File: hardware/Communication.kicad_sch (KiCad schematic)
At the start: 28 parts, among them J1 Conn_01x04_Pin, J2 Conn_01x03_Male, J3 USB_C_Receptacle_USB2.0, U21 TXB0102DCT, U22 ADUM4160

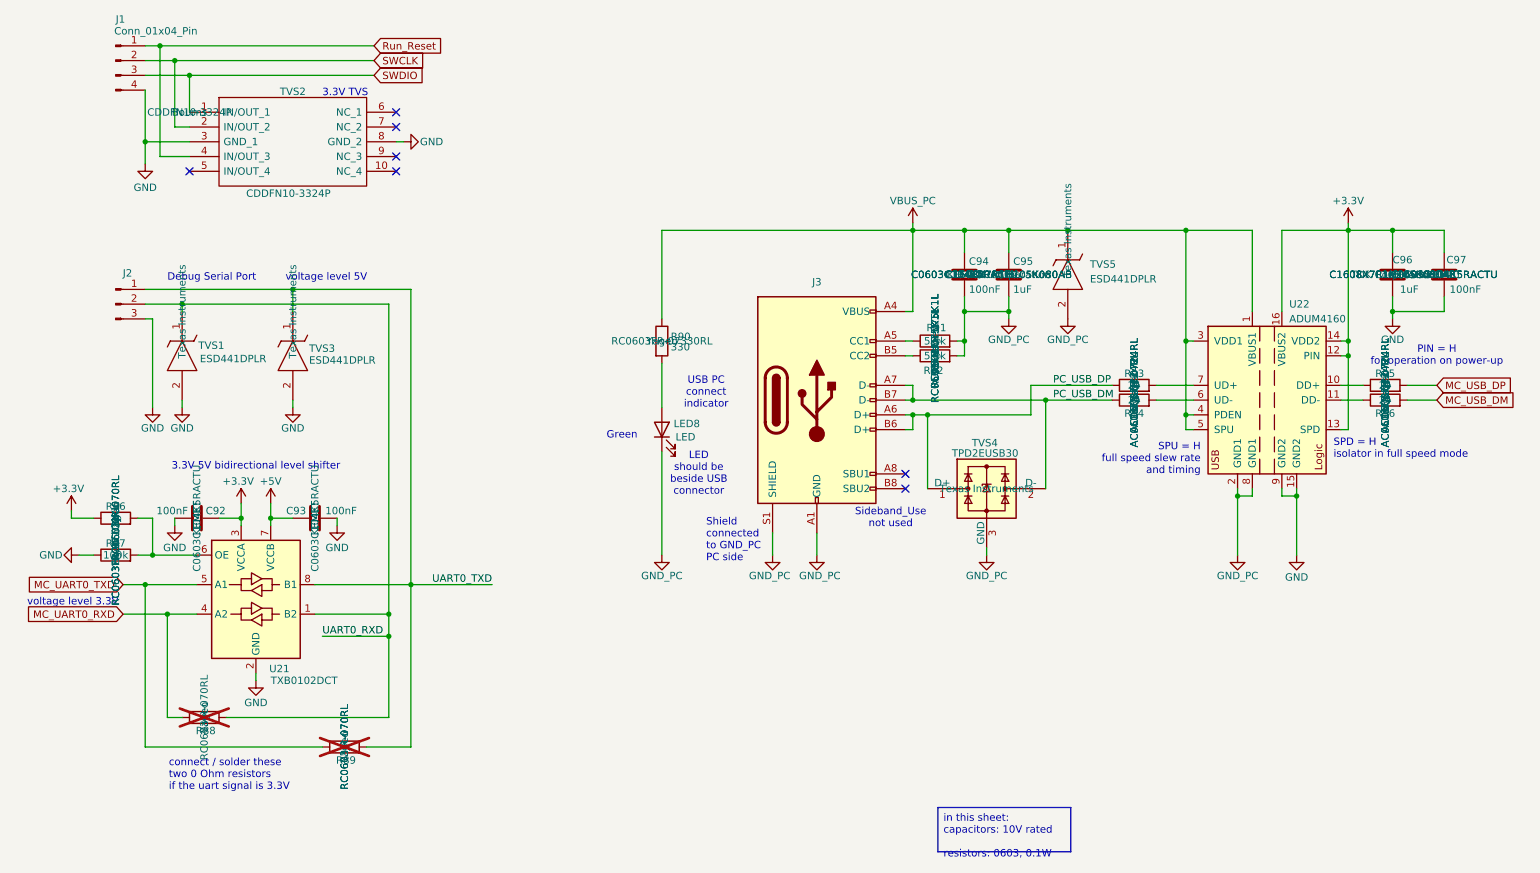
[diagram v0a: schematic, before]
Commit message: Not necessary text is hidden + BOM on schematic
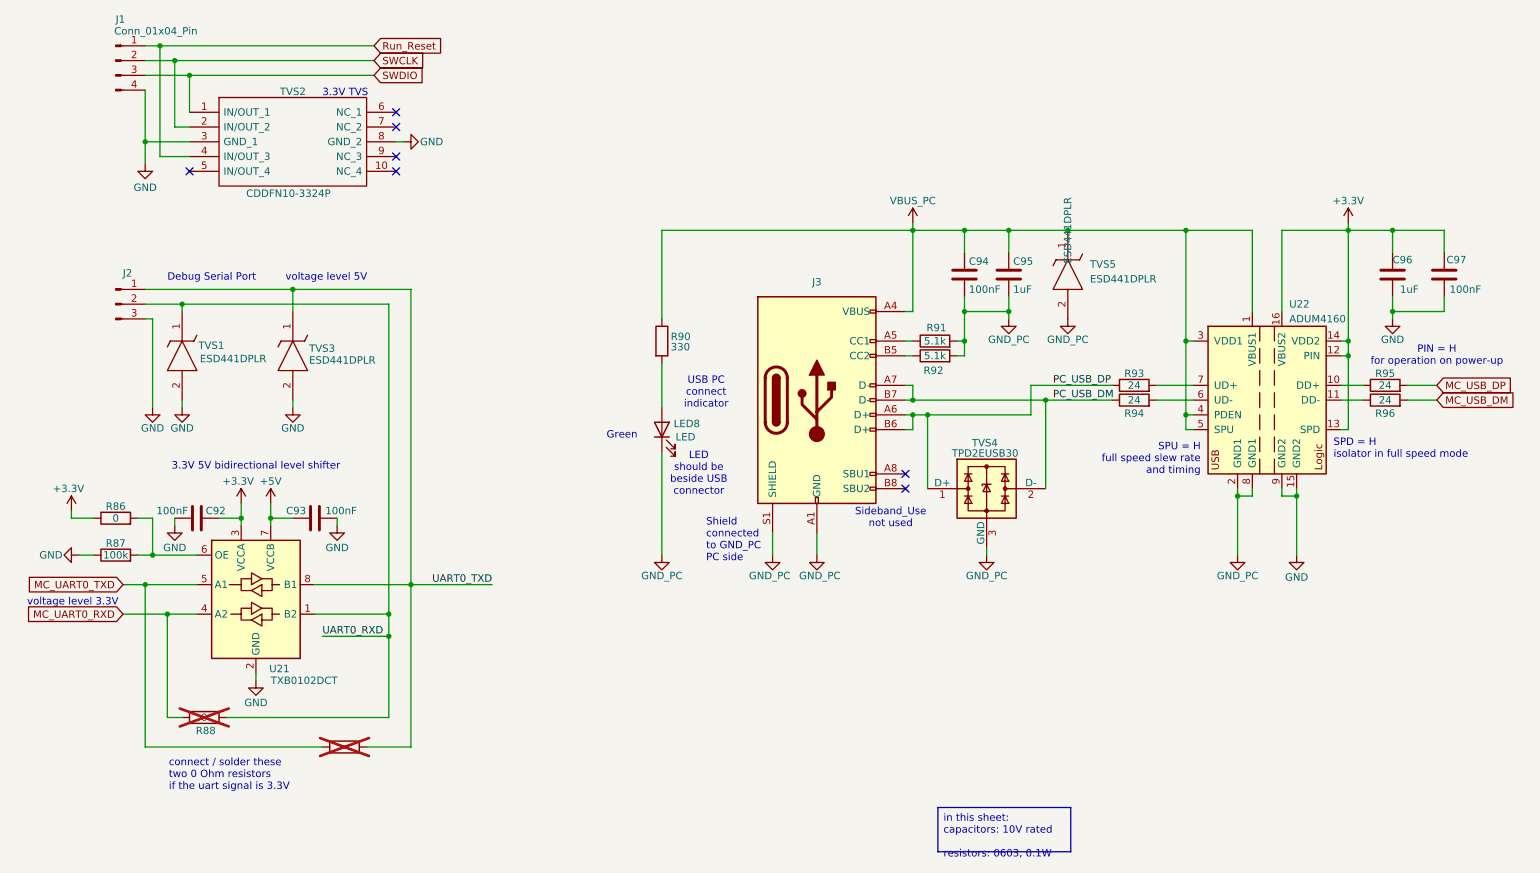
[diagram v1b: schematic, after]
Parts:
- C92, C93, C94, C97: Temperature Coefficient X7R -> (none)
- C95, C96: Temperature Coefficient X5R -> (none)
- LED8: Manufacturer_Part_Number (none) -> XZCDGK53W-1VF
- TVS1, TVS3, TVS5: MPN (none) -> ESD441DPLR
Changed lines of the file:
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@@
 					(size 1.27 1.27)
 				)
+				(hide yes)
 			)
 		)
@@
 					(size 1.27 1.27)
 				)
+				(hide yes)
 			)
 		)
@@
 					(size 1.27 1.27)
 				)
+				(hide yes)
 			)
 		)
@@
 					(size 1.27 1.27)
 				)
+				(hide yes)
 			)
 		)
@@
 					(size 1.27 1.27)
 				)
+				(hide yes)
 			)
 		)
@@
 					(size 1.27 1.27)
 				)
+				(hide yes)
 			)
 		)
@@
 					(size 1.27 1.27)
 				)
+				(hide yes)
+			)
+		)
+		(property "MPN" "ESD441DPLR"
+			(at 46.99 72.39 0)
+			(effects
+				(font
+					(size 1.27 1.27)
+				)
+				(hide yes)
 			)
 		)
@@
 					(size 1.27 1.27)
 				)
+				(hide yes)
+			)
+		)
+		(property "MPN" "ESD441DPLR"
+			(at 66.04 72.39 0)
+			(effects
+				(font
+					(size 1.27 1.27)
+				)
+				(hide yes)
 			)
 		)
@@
 					(size 1.27 1.27)
 				)
+				(hide yes)
 			)
 		)
@@
 					(size 1.27 1.27)
 				)
+				(hide yes)
 			)
 		)
@@
 					(size 1.27 1.27)
 				)
+				(hide yes)
 			)
 		)
@@
 			)
 		)
-		(property "Temperature Coefficient" "X7R"
+		(property "Temperature Coefficient" ""
 			(at 49.53 107.95 0)
 			(effects
@@
 					(size 1.27 1.27)
 				)
+				(hide yes)
 			)
 		)
@@
 					(size 1.27 1.27)
 				)
+				(hide yes)
 			)
 		)
@@
 					(size 1.27 1.27)
 				)
+				(hide yes)
 			)
 		)
@@
 					(size 1.27 1.27)
 				)
+				(hide yes)
+			)
+		)
+		(property "MPN" "ESD441DPLR"
+			(at 199.39 58.42 0)
+			(effects
+				(font
+					(size 1.27 1.27)
+				)
 			)
 		)
@@
 					(size 1.27 1.27)
 				)
+				(hide yes)
 			)
 		)
@@
 					(size 1.27 1.27)
 				)
+				(hide yes)
 			)
 		)
@@
 					(size 1.27 1.27)
 				)
+				(hide yes)
 			)
 		)
@@
 					(size 1.27 1.27)
 				)
+				(hide yes)
 			)
 		)
@@
 					(size 1.27 1.27)
 				)
+				(hide yes)
 			)
 		)
@@
 					(size 1.27 1.27)
 				)
+				(hide yes)
 			)
 		)
@@
 					(size 1.27 1.27)
 				)
+				(hide yes)
 			)
 		)
@@
 					(size 1.27 1.27)
 				)
+				(hide yes)
 			)
 		)
@@
 					(size 1.27 1.27)
 				)
+				(hide yes)
 			)
 		)
@@
 					(size 1.27 1.27)
 				)
+				(hide yes)
 			)
 		)
@@
 					(size 1.27 1.27)
 				)
+				(hide yes)
 			)
 		)
@@
 					(size 1.27 1.27)
 				)
+				(hide yes)
 			)
 		)
@@
 					(size 1.27 1.27)
 				)
+				(hide yes)
 			)
 		)
@@
 					(size 1.27 1.27)
 				)
+				(hide yes)
 			)
 		)
@@
 			)
 		)
-		(property "Temperature Coefficient" "X7R"
+		(property "Temperature Coefficient" ""
 			(at 264.16 66.04 0)
 			(effects
@@
 					(size 1.27 1.27)
 				)
+				(hide yes)
 			)
 		)
@@
 					(size 1.27 1.27)
 				)
+				(hide yes)
 			)
 		)
@@
 					(size 1.27 1.27)
 				)
+				(hide yes)
 			)
 		)
@@
 					(size 1.27 1.27)
 				)
+				(hide yes)
 			)
 		)
@@
 					(size 1.27 1.27)
 				)
+				(hide yes)
 			)
 		)
@@
 					(size 1.27 1.27)
 				)
+				(hide yes)
 			)
 		)
@@
 					(size 1.27 1.27)
 				)
+				(hide yes)
 			)
 		)
@@
 					(size 1.27 1.27)
 				)
+				(hide yes)
 			)
 		)
@@
 					(size 1.27 1.27)
 				)
+				(hide yes)
 			)
 		)
@@
 					(size 1.27 1.27)
 				)
+				(hide yes)
 			)
 		)
@@
 			)
 		)
-		(property "Temperature Coefficient" "X5R"
+		(property "Temperature Coefficient" ""
 			(at 255.27 66.04 0)
 			(effects
@@
 					(size 1.27 1.27)
 				)
+				(hide yes)
 			)
 		)
@@
 					(size 1.27 1.27)
 				)
+				(hide yes)
 			)
 		)
@@
 					(size 1.27 1.27)
 				)
+				(hide yes)
 			)
 		)
@@
 					(size 1.27 1.27)
 				)
+				(hide yes)
 			)
 		)
@@
 					(size 1.27 1.27)
 				)
+				(hide yes)
 			)
 		)
@@
 					(size 1.27 1.27)
 				)
+				(hide yes)
 			)
 		)
@@
 					(size 1.27 1.27)
 				)
+				(hide yes)
 			)
 		)
@@
 			)
 		)
-		(property "Temperature Coefficient" "X7R"
+		(property "Temperature Coefficient" ""
 			(at 181.61 66.04 0)
 			(effects
@@
 					(size 1.27 1.27)
 				)
+				(hide yes)
 			)
 		)
@@
 					(size 1.27 1.27)
 				)
+				(hide yes)
 			)
 		)
@@
 					(size 1.27 1.27)
 				)
+				(hide yes)
 			)
 		)
@@
 			)
 		)
+		(property "Manufacturer_Part_Number" "XZCDGK53W-1VF"
+			(at 126.746 92.456 0)
+			(effects
+				(font
+					(size 1.27 1.27)
+				)
+				(hide yes)
+			)
+		)
 		(pin "1"
 		)
@@
 			)
 		)
-		(property "Temperature Coefficient" "X5R"
+		(property "Temperature Coefficient" ""
 			(at 189.23 66.04 0)
 			(effects
@@
 					(size 1.27 1.27)
 				)
+				(hide yes)
 			)
 		)
@@
 					(size 1.27 1.27)
 				)
+				(hide yes)
 			)
 		)
@@
 					(size 1.27 1.27)
 				)
+				(hide yes)
 			)
 		)
@@
 					(size 1.27 1.27)
 				)
+				(hide yes)
 			)
 		)
@@
 			)
 		)
-		(property "Temperature Coefficient" "X7R"
+		(property "Temperature Coefficient" ""
 			(at 69.85 107.95 0)
 			(effects
@@
 					(size 1.27 1.27)
 				)
+				(hide yes)
 			)
 		)
@@
 					(size 1.27 1.27)
 				)
+				(hide yes)
 			)
 		)
@@
 					(size 1.27 1.27)
 				)
+				(hide yes)
 			)
 		)
@@
 					(size 1.27 1.27)
 				)
+				(hide yes)
 			)
 		)

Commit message: BOM cont.
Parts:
- J1: Link (none) -> n/a; MPN (none) -> n/a; Manufacturer (none) -> n/a; Manufacturer_Name (none) -> n/a; Manufacturer_Part_Number (none) -> n/a
- J2: MPN (none) -> n/a; Manufacturer_Name (none) -> n/a; Manufacturer_Part_Number (none) -> n/a
- J3: MPN (none) -> DX07S016JA1R1500; Manufacturer_Name (none) -> JAE Electronics; Manufacturer_Part_Number (none) -> DX07S016JA1R1500
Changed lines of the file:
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@@
 	(text "voltage level 5V"
 		(exclude_from_sim no)
-		(at 64.77 67.31 0)
+		(at 70.358 68.072 0)
 		(effects
 			(font
@@
 	(text "Debug Serial Port"
 		(exclude_from_sim no)
-		(at 44.45 67.31 0)
+		(at 48.26 68.072 0)
 		(effects
 			(font
@@
 			)
 		)
+		(property "Link" "n/a"
+			(at 35.56 29.21 0)
+			(effects
+				(font
+					(size 1.27 1.27)
+				)
+				(hide yes)
+			)
+		)
+		(property "Manufacturer" "n/a"
+			(at 35.56 29.21 0)
+			(effects
+				(font
+					(size 1.27 1.27)
+				)
+				(hide yes)
+			)
+		)
+		(property "Manufacturer_Part_Number" "n/a"
+			(at 35.56 29.21 0)
+			(effects
+				(font
+					(size 1.27 1.27)
+				)
+				(hide yes)
+			)
+		)
+		(property "MPN" "n/a"
+			(at 35.56 29.21 0)
+			(effects
+				(font
+					(size 1.27 1.27)
+				)
+				(hide yes)
+			)
+		)
+		(property "Manufacturer_Name" "n/a"
+			(at 35.56 29.21 0)
+			(effects
+				(font
+					(size 1.27 1.27)
+				)
+				(hide yes)
+			)
+		)
 		(pin "2"
 		)
@@
 		(dnp no)
 		(property "Reference" "J2"
-			(at 37.592 65.786 0)
+			(at 37.084 62.484 0)
 			(effects
 				(font
@@
 		)
 		(property "Value" "Conn_01x03_Male"
-			(at 36.195 66.04 0)
+			(at 35.56 65.024 0)
 			(effects
 				(font
 					(size 1.27 1.27)
 				)
-				(hide yes)
+				(justify left)
 			)
 		)
@@
 			)
 		)
+		(property "Manufacturer_Part_Number" "n/a"
+			(at 35.56 71.12 0)
+			(effects
+				(font
+					(size 1.27 1.27)
+				)
+				(hide yes)
+			)
+		)
+		(property "MPN" "n/a"
+			(at 35.56 71.12 0)
+			(effects
+				(font
+					(size 1.27 1.27)
+				)
+				(hide yes)
+			)
+		)
+		(property "Manufacturer_Name" "n/a"
+			(at 35.56 71.12 0)
+			(effects
+				(font
+					(size 1.27 1.27)
+				)
+				(hide yes)
+			)
+		)
 		(pin "1"
 		)
@@
 		(on_board yes)
 		(dnp no)
-		(fields_autoplaced yes)
 		(property "Reference" "J3"
 			(at 156.21 67.31 0)
@@
 		)
 		(property "Value" "USB_C_Receptacle_USB2.0"
-			(at 156.21 67.31 0)
+			(at 155.956 68.834 0)
 			(effects
 				(font
 					(size 1.27 1.27)
 				)
-				(hide yes)
 			)
 		)
@@
 			(at 156.21 87.63 0)
 			(effects
+				(font
+					(size 1.27 1.27)
+				)
+				(hide yes)
+			)
+		)
+		(property "Manufacturer_Part_Number" "DX07S016JA1R1500"
+			(at 156.21 87.63 0)
+			(effects
+				(font
+					(size 1.27 1.27)
+				)
+				(hide yes)
+			)
+		)
+		(property "MPN" "DX07S016JA1R1500"
+			(at 156.21 87.63 0)
+			(effects
+				(font
+					(size 1.27 1.27)
+				)
+				(hide yes)
+			)
+		)
+		(property "Manufacturer_Name" "JAE Electronics"
+			(at 156.21 87.63 0)
+			(effects

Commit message: TVS16,TVS17,TVS18,TVS19 parts have been changed from ESDSB12VLB-TP to PESD12VL1BSLAZ
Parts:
- TVS2: footprint CDDFN103324P -> harp.device.quad.dac.kicad:CDDFN103324P
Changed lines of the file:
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@@
 			)
 		)
-		(property "Footprint" "CDDFN103324P"
+		(property "Footprint" "harp.device.quad.dac.kicad:CDDFN103324P"
 			(at 80.01 35.56 0)
 			(effects

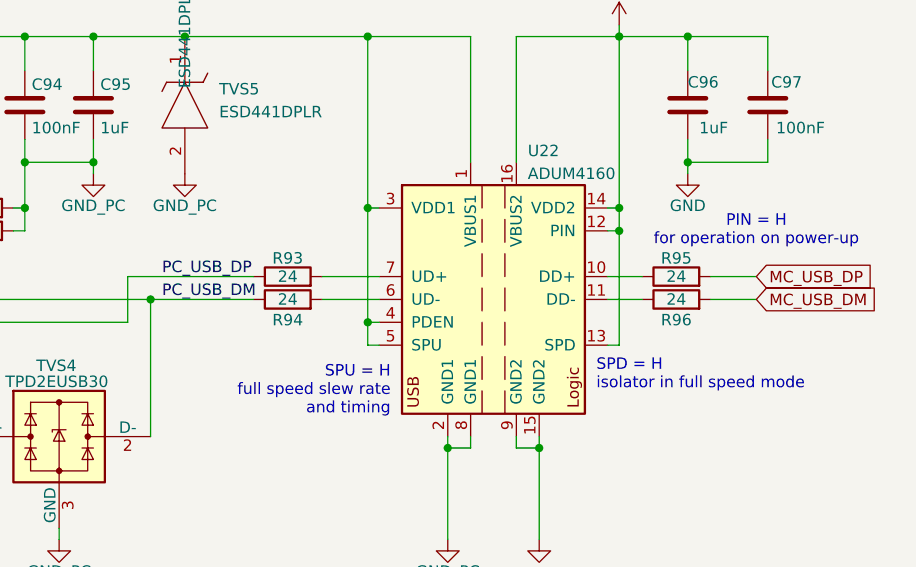
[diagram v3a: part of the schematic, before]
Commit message: Rename Some nets
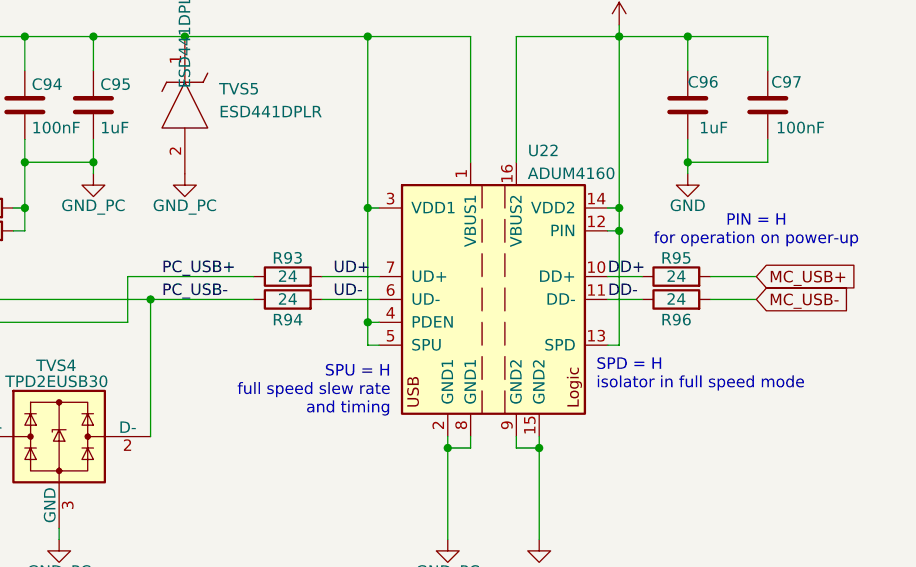
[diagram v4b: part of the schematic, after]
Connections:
- net DD-: now reaches R96.1, U22.11 (DD-)
- net UD-: now reaches R94.2, U22.6 (UD-)
- net DD+: now reaches R95.1, U22.10 (DD+)
- net UD+: now reaches R93.2, U22.7 (UD+)
- net MC_USB_DM renamed MC_USB-
- net MC_USB_DP renamed MC_USB+
- net PC_USB_DM renamed PC_USB-
- net PC_USB_DP renamed PC_USB+
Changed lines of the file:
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@@
+		)
+	)
+	(label "DD-"
+		(at 246.4062 87.63 0)
+		(effects
+			(font
+				(size 1.27 1.27)
+			)
+			(justify left bottom)
+		)
+	)
+	(label "DD+"
+		(at 246.38 85.09 0)
+		(effects
+			(font
+				(size 1.27 1.27)
+			)
+			(justify left bottom)
 		)
 	)
@@
 		)
 	)
-	(label "PC_USB_DM"
+	(label "UD+"
+		(at 215.9 85.09 0)
+		(effects
+			(font
+				(size 1.27 1.27)
+			)
+			(justify left bottom)
+		)
+	)
+	(label "PC_USB-"
 		(at 196.85 87.63 0)
 		(effects
@@
 		)
 	)
-	(label "PC_USB_DP"
+	(label "PC_USB+"
 		(at 196.85 85.09 0)
+		(effects
+			(font
+				(size 1.27 1.27)
+			)
+			(justify left bottom)
+		)
+	)
+	(label "UD-"
+		(at 215.9 87.63 0)
 		(effects
 			(font
@@
 		)
 	)
-	(global_label "MC_USB_DM"
+	(global_label "MC_USB-"
 		(shape input)
 		(at 262.89 87.63 0)
@@
 		)
 		(property "Intersheetrefs" "${INTERSHEET_REFS}"
-			(at 277.0632 87.63 0)
+			(at 274.9466 87.63 0)
 			(effects
 				(font
@@
 		)
 	)
-	(global_label "MC_USB_DP"
+	(global_label "MC_USB+"
 		(shape input)
 		(at 262.89 85.09 0)
@@
 		)
 		(property "Intersheetrefs" "${INTERSHEET_REFS}"
-			(at 276.8818 85.09 0)
+			(at 274.9466 85.09 0)
 			(effects
 				(font

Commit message: The layout is complete, and the design is currently in the review stage.
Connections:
- net SWCLK: now also J1.3 (Pin_3), TVS2.1 (IN/OUT_1); no longer J1.2 (Pin_2), TVS2.2 (IN/OUT_2)
- net SWDIO: now also J1.2 (Pin_2), TVS2.2 (IN/OUT_2); no longer J1.3 (Pin_3), TVS2.1 (IN/OUT_1)

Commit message: Continue BOM + enhance BOM + enhance schematic
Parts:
- C95, C96: Manufacturer TDK Corporation -> TDK; Manufacturer_Name TDK Corporation -> TDK
- LED8: Manufacturer_Name (none) -> SunLED
- TVS1, TVS3, TVS5: Link (none) -> https://www.digikey.com/en/products/detail/texas-instrument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
- TVS2: Link (none) -> https://www.digikey.com/en/products/detail/bourns-inc/CDDFN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
- TVS4: MPN (none) -> TPD2EUSB30DRTR; Manufacturer_Part_Number (none) -> TPD2EUSB30DRTR
- U21: value TXB0102DCT -> TXB0102DCUT; Link (none) -> https://www.digikey.com/en/products/detail/texas-instrument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; MPN (none) -> TXB0102DCUT; Manufacturer (none) -> Texas Instruments; Manufacturer_Name (none) -> Texas Instruments; Manufacturer_Part_Number (none) -> TXB0102DCUT
- U22: MPN (none) -> ADUM4160BRWZ-RL; Manufacturer Analog Devices Inc. -> Analog Devices; Manufacturer_Name (none) -> Analog Devices; Manufacturer_Part_Number (none) -> ADUM4160BRWZ-RL
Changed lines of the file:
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@@
 			)
 		)
+		(property "Link" "https://www.digikey.com/en/products/detail/texas-instruments/ESD441DPLR/21298753"
+			(at 46.99 72.39 0)
+			(effects
+				(font
+					(size 1.27 1.27)
+				)
+				(hide yes)
+			)
+		)
 		(pin "2"
 		)
@@
 			)
 		)
+		(property "Link" "https://www.digikey.com/en/products/detail/texas-instruments/ESD441DPLR/21298753"
+			(at 66.04 72.39 0)
+			(effects
+				(font
+					(size 1.27 1.27)
+				)
+				(hide yes)
+			)
+		)
 		(pin "2"
 		)
@@
 			)
 		)
+		(property "MPN" "TPD2EUSB30DRTR"
+			(at 185.42 102.87 0)
+			(effects
+				(font
+					(size 1.27 1.27)
+				)
+				(hide yes)
+			)
+		)
+		(property "Manufacturer_Part_Number" "TPD2EUSB30DRTR"
+			(at 185.42 102.87 0)
+			(effects
+				(font
+					(size 1.27 1.27)
+				)
+				(hide yes)
+			)
+		)
 		(pin "1"
 		)
@@
 					(size 1.27 1.27)
 				)
+				(hide yes)
+			)
+		)
+		(property "Link" "https://www.digikey.com/en/products/detail/texas-instruments/ESD441DPLR/21298753"
+			(at 199.39 58.42 0)
+			(effects
+				(font
+					(size 1.27 1.27)
+				)
+				(hide yes)
 			)
 		)
@@
 			)
 		)
-		(property "Value" "TXB0102DCT"
+		(property "Value" "TXB0102DCUT"
 			(at 62.23 135.89 0)
 			(effects
@@
 			)
 		)
+		(property "Link" "https://www.digikey.com/en/products/detail/texas-instruments/TXB0102DCUT/1910149"
+			(at 59.69 121.92 0)
+			(effects
+				(font
+					(size 1.27 1.27)
+				)
+				(hide yes)
+			)
+		)
+		(property "MPN" "TXB0102DCUT"
+			(at 59.69 121.92 0)
+			(effects
+				(font
+					(size 1.27 1.27)
+				)
+				(hide yes)
+			)
+		)
+		(property "Manufacturer" "Texas Instruments"
+			(at 59.69 121.92 0)
+			(effects
+				(font
+					(size 1.27 1.27)
+				)
+				(hide yes)
+			)
+		)
+		(property "Manufacturer_Name" "Texas Instruments"
+			(at 59.69 121.92 0)
+			(effects
+				(font
+					(size 1.27 1.27)
+				)
+				(hide yes)
+			)
+		)
+		(property "Manufacturer_Part_Number" "TXB0102DCUT"
+			(at 59.69 121.92 0)
+			(effects
+				(font
+					(size 1.27 1.27)
+				)
+				(hide yes)
+			)
+		)
 		(pin "4"
 		)
@@
 			)
 		)
-		(property "Manufacturer" "TDK Corporation"
+		(property "Manufacturer" "TDK"
 			(at 255.27 66.04 0)
 			(effects
@@
 			)
 		)
-		(property "Manufacturer_Name" "TDK Corporation"
+		(property "Manufacturer_Name" "TDK"
 			(at 255.27 66.04 0)
 			(effects
@@
 			)
 		)
-		(property "Manufacturer" "Analog Devices Inc."
+		(property "Manufacturer" "Analog Devices"
+			(at 233.68 87.63 0)
+			(effects
+				(font
+					(size 1.27 1.27)
+				)
+				(hide yes)
+			)
+		)
+		(property "MPN" "ADUM4160BRWZ-RL"
+			(at 233.68 87.63 0)
+			(effects
+				(font
+					(size 1.27 1.27)
+				)
+				(hide yes)
+			)
+		)
+		(property "Manufacturer_Name" "Analog Devices"
+			(at 233.68 87.63 0)
+			(effects
+				(font
+					(size 1.27 1.27)
+				)
+				(hide yes)
+			)
+		)
+		(property "Manufacturer_Part_Number" "ADUM4160BRWZ-RL"
 			(at 233.68 87.63 0)
 			(effects
@@
 			)
 		)
+		(property "Manufacturer_Name" "SunLED"
+			(at 129.54 92.71 0)
+			(effects
+				(font
+					(size 1.27 1.27)
+				)
+				(hide yes)
+			)
+		)
 		(pin "1"
 		)
@@
 			)
 		)
-		(property "Manufacturer" "TDK Corporation"
+		(property "Manufacturer" "TDK"
 			(at 189.23 66.04 0)
 			(effects
@@
 			)
 		)
-		(property "Manufacturer_Name" "TDK Corporation"
+		(property "Manufacturer_Name" "TDK"
 			(at 189.23 66.04 0)
 			(effects
@@
 			(at 48.26 38.1 0)
 			(effects
+				(font
+					(size 1.27 1.27)
+				)
+				(hide yes)
+			)
+		)
+		(property "Link" "https://www.digikey.com/en/products/detail/bourns-inc/CDDFN10-3324P/5019648"
+			(at 48.26 38.1 0)
+			(effects
